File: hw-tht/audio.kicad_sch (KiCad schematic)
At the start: 13 parts, among them U9 PCM5100A

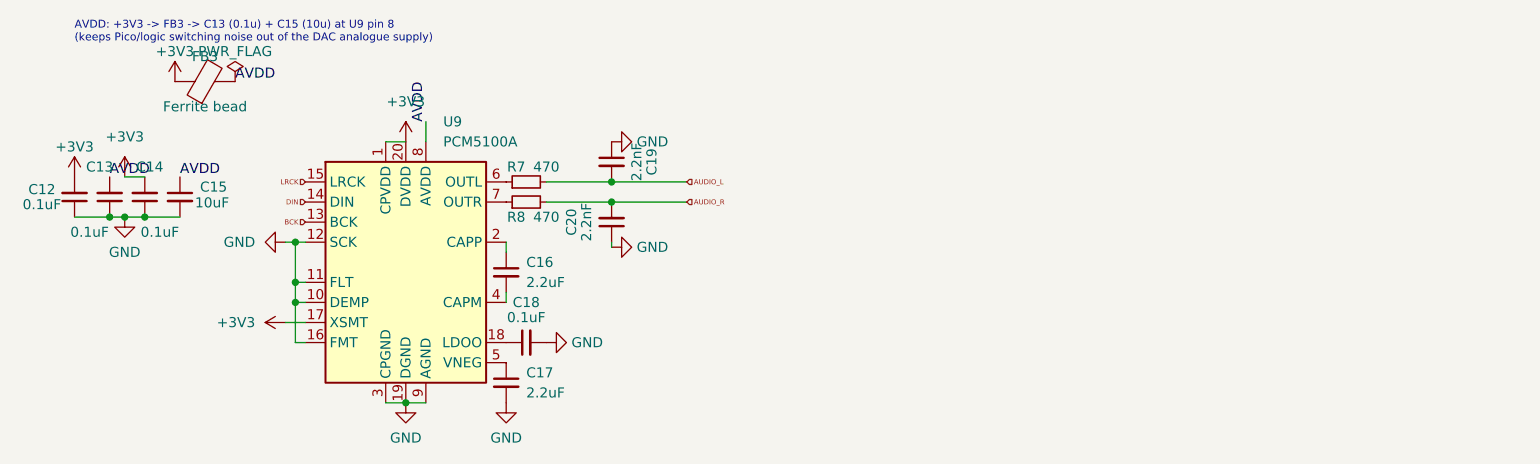
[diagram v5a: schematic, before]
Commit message: hw-tht: GY-PCM5102 module option (J10) as an either/or alternative to the DAC
- J10 (new footprint PiGUS library:GY-PCM5102_Module + symbol): the module plugs
  in on female headers - its I2S row (SCK->GND, BCK, DIN, LCK, GND, VIN=+5V) and
  the AGND/ROUT/AGND/LROUT end of its 9-pin row, as I2S_DAC1/J4 on v1.2. Its
  outputs join U9's (DAC_OUTL/R) ahead of R7/R8 + C19/C20, so the mixer, WT path
  and firmware are unchanged. Fit U9 + C12-C18 + FB3 OR the module, never both.
- Placed right of the Waveblaster area over low parts (courtyard only around the
  pins); R4 and C28 moved a few mm. Oval pads keep two tracks per gap.
- Silkscreen: dashed "DAC" outline around the parts to leave out for the module
  (R7/R8 notched out: they stay), heading "DAC -OR- J10 MODULE", dashed module
  outline labelled "J10: GY-PCM5102".
- BOM: J10 module + 1x6/1x4 female headers as optional lines; U9 note.
- README: DAC option section with the fit/leave-out table.
- Re-routed around the module: 0 DRC errors, 0 unconnected, schematic parity OK;
  ERC 0 errors.

Co-Authored-By: Claude Opus 5.5 <noreply@anthropic.com>
Claude-Session: https://claude.ai/code/session_011utN3x8yYUNDvkpGCEq5yD
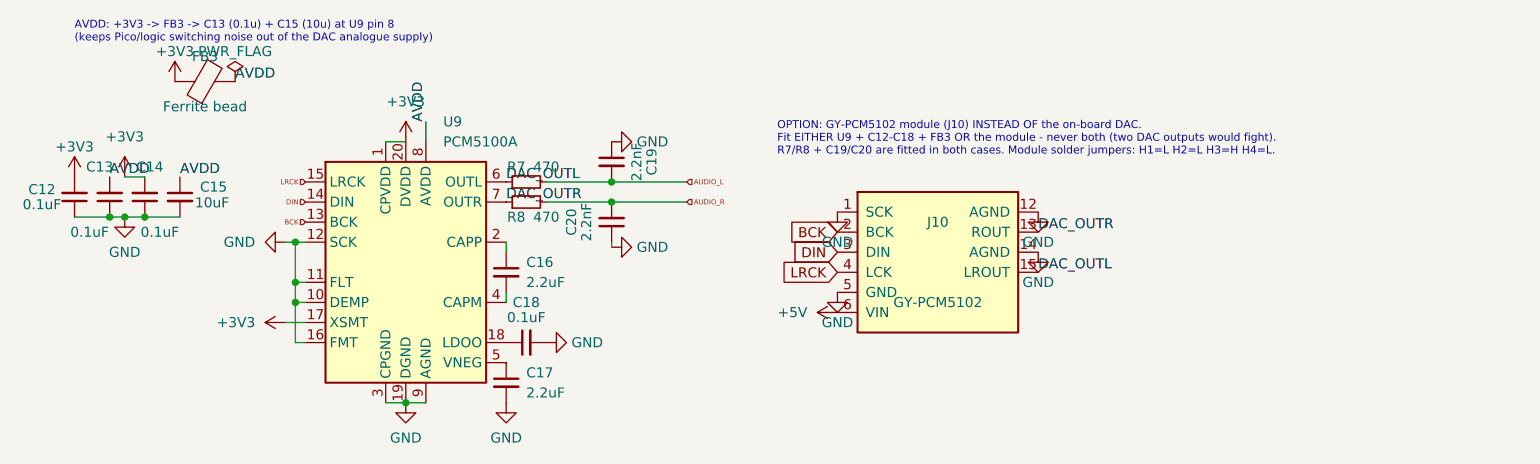
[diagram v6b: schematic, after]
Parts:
- added J10: GY-PCM5102, PiGUS library:GY-PCM5102_Module, symbol PiGUS library:GY-PCM5102
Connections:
- net BCK: now also J10.2 (BCK)
- net DIN: now also J10.3 (DIN)
- net GND: now also J10.1 (SCK), J10.12 (AGND), J10.14 (AGND), J10.5 (GND)
- net LRCK: now also J10.4 (LCK)
- net DAC_OUTL: now reaches R7.1, U9.6 (OUTL)
- net DAC_OUTL: now also J10.15 (LROUT)
- net DAC_OUTR: now reaches R8.1, U9.7 (OUTR)
- net DAC_OUTR: now also J10.13 (ROUT)
- new net +5V: J10.6 (VIN)
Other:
- note added: "OPTION: GY-PCM5102 module (J10) INSTEAD OF the on-board DAC. Fit EITHER U9 + C12-C18 + FB3 OR the module - never both (two DAC outputs would fight). R7/R8 + C19/C20 are fitted in both cases. Module solder jumpers: H1=L H2=L H3=H H4=L."

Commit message: hw-tht: R7/R8 + C19/C20 belong to the DAC area; module feeds AUDIO_L/R
The GY-PCM5102 module already has the PCM510x reference 470R/2.2nF output
filter, so J10's ROUT/LROUT now join AUDIO_L/R after R7/R8 + C19/C20 instead of
U9's outputs. The whole filter is left out with the DAC when the module is used
(no double filter, no extra 470R in front of the mixer).

- Dashed DAC outline now encloses U9, C12-C20, FB3, R7, R8 (steps under J10's
  pin row); "J10: GY-PCM5102" label moved inside the module outline.
- Schematic note, BOM notes and README table updated.
- Re-routed the four audio nets: 0 DRC errors, 0 unconnected, parity OK; ERC 0.

Co-Authored-By: Claude Opus 5.5 <noreply@anthropic.com>
Claude-Session: https://claude.ai/code/session_011utN3x8yYUNDvkpGCEq5yD
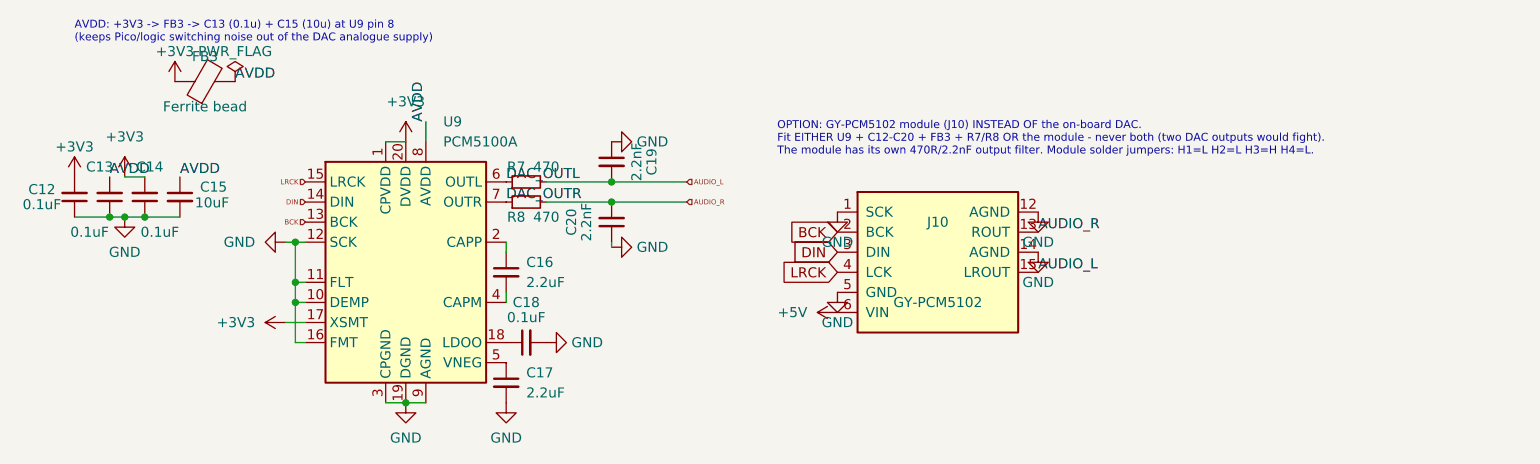
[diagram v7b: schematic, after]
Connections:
- net AUDIO_L: now also J10.15 (LROUT)
- net AUDIO_R: now also J10.13 (ROUT)
- net DAC_OUTL: no longer J10.15 (LROUT)
- net DAC_OUTR: no longer J10.13 (ROUT)
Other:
- note added: "OPTION: GY-PCM5102 module (J10) INSTEAD OF the on-board DAC. Fit EITHER U9 + C12-C20 + FB3 + R7/R8 OR the module - never both (two DAC outputs would fight). The module has its own 470R/2.2nF output filter. Module solder jumpers: H1=L H2=L H3=H H4=L."
- note removed: "OPTION: GY-PCM5102 module (J10) INSTEAD OF the on-board DAC. Fit EITHER U9 + C12-C18 + FB3 OR the module - never both (two DAC outputs would fight). R7/R8 + C19/C20 are fitted in both cases. Module solder jumpers: H1=L H2=L H3=H H4=L."
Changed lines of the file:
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@@
 			)
 		)
-		(property "Description" "OPTIONAL GY-PCM5102 DAC module on female headers, INSTEAD OF U9 + C12-C18 + FB3 (the DAC area). Fit one or the other, never both."
+		(property "Description" "OPTIONAL GY-PCM5102 DAC module on female headers, INSTEAD OF the DAC area: U9, C12-C20, FB3, R7, R8. Fit one or the other, never both."
 			(at 132.08 55.88 0)
 			(hide yes)
@@
 		)
 	)
-	(label "DAC_OUTR"
+	(label "AUDIO_R"
 		(at 144.78 52.07 0)
 		(effects
@@
 		)
 	)
-	(label "DAC_OUTL"
+	(label "AUDIO_L"
 		(at 144.78 57.15 0)
 		(effects
@@
 		)
 	)
-	(text "OPTION: GY-PCM5102 module (J10) INSTEAD OF the on-board DAC.\nFit EITHER U9 + C12-C18 + FB3 OR the module - never both (two DAC outputs would fight).\nR7/R8 + C19/C20 are fitted in both cases. Module solder jumpers: H1=L H2=L H3=H H4=L."
+	(text "OPTION: GY-PCM5102 module (J10) INSTEAD OF the on-board DAC.\nFit EITHER U9 + C12-C20 + FB3 + R7/R8 OR the module - never both (two DAC outputs would fight).\nThe module has its own 470R/2.2nF output filter. Module solder jumpers: H1=L H2=L H3=H H4=L."
 		(exclude_from_sim no)
 		(at 111.76 38.1 0)
